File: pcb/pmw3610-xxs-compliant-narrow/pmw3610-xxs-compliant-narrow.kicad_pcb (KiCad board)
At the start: 2 copper layers, 16 x 42 mm, 21 parts, among them J2 vik-module-connector, U1 MCP1700T-1802E/TT, U2 PMW3610

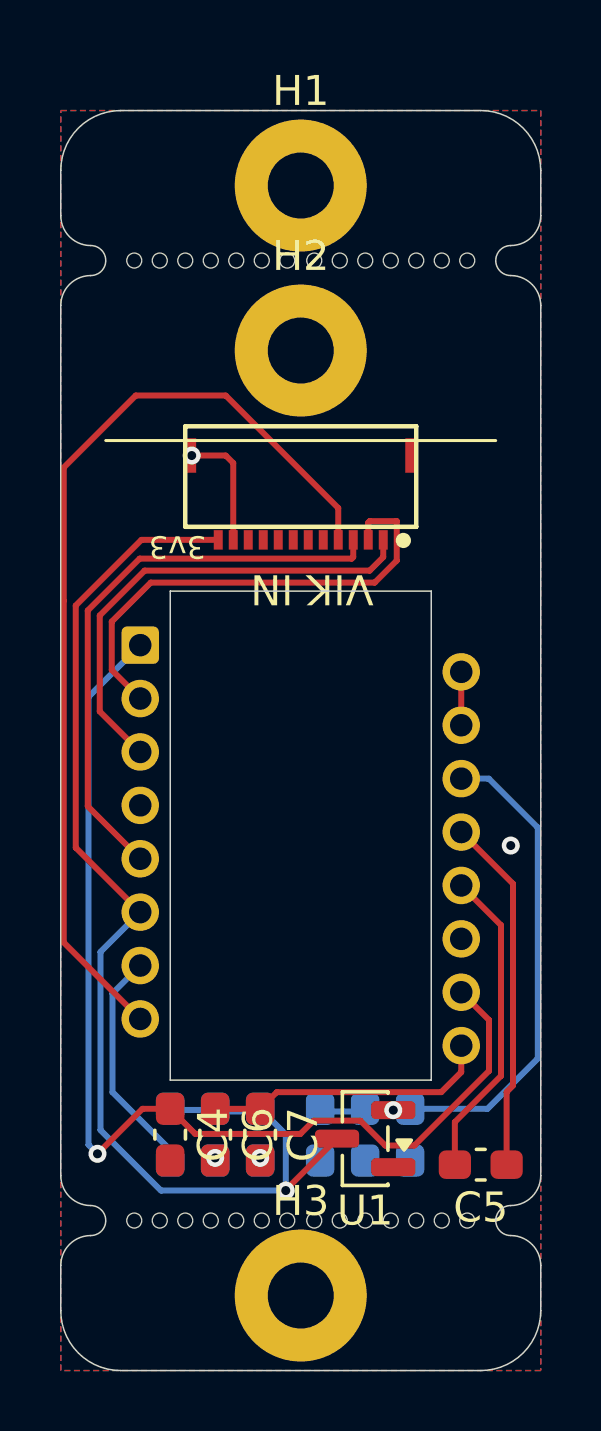
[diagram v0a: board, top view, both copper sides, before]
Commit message: Reduce PMW-3610-narrow PCB width from 16mm to 15mm.
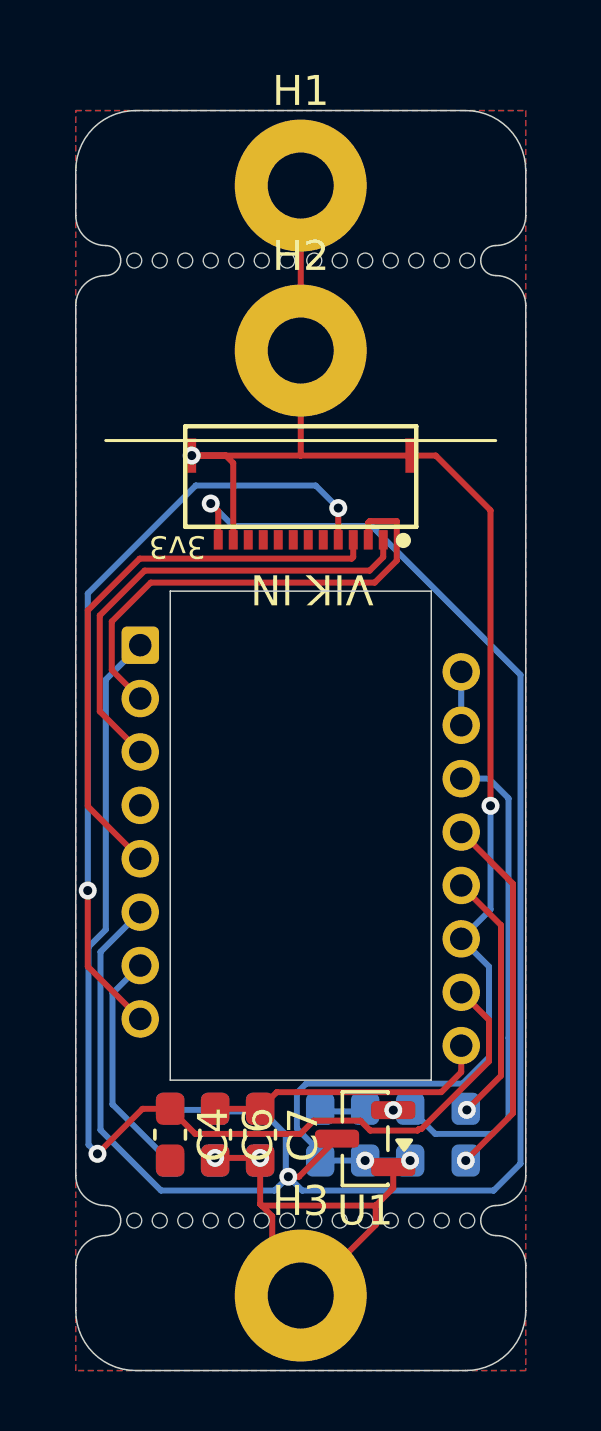
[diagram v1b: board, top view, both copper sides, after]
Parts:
- C5: moved to B.Cu
- moved REF** 4.37 mm to (33.0, 30.0)
- moved C5 1.12 mm to (33.5, 54.1), turned to 90 degrees
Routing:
- net GND: track 4.05 -> 71.4 mm, vias 4 -> 6
- net VCC: track 40.2 -> 61.6 mm, vias 1 -> 2
- net MOTION: track 32.2 -> 26.1 mm, vias 0 -> 2
- net Net-(U2-CP): track 10.5 -> 8.55 mm, vias 0 -> 1
- net Net-(U2-+VCSEL): track 36.4 -> 35.8 mm
- net Net-(U2-CN): track 11.9 -> 12.3 mm, vias 0 -> 1
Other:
- board size 16 x 42 mm -> 15 x 42 mm
